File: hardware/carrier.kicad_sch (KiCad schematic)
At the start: 22 parts, among them J1 OPI_Z3_26PIN, J10 AUX 5V (screen), J14 BUCK 5V, J16 BATT 12V, J2 OPI_BREAKOUT, J3 UART5 ttyAS5, J4 UART2 ttyAS2, J8 I2C3 spare, J9 FAN 5V, Q1 IRF9540N

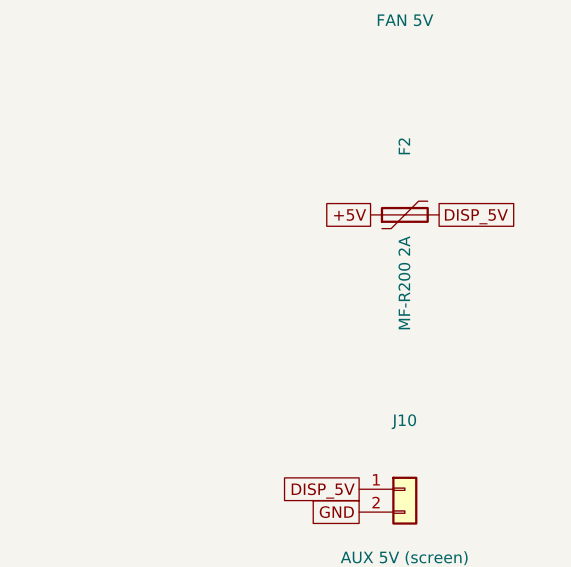
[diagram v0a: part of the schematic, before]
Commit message: chore: F2 MF-R200 -> MF-R250 (2.5A hold, same footprint)
Co-Authored-By: Claude Fable 5 <noreply@anthropic.com>
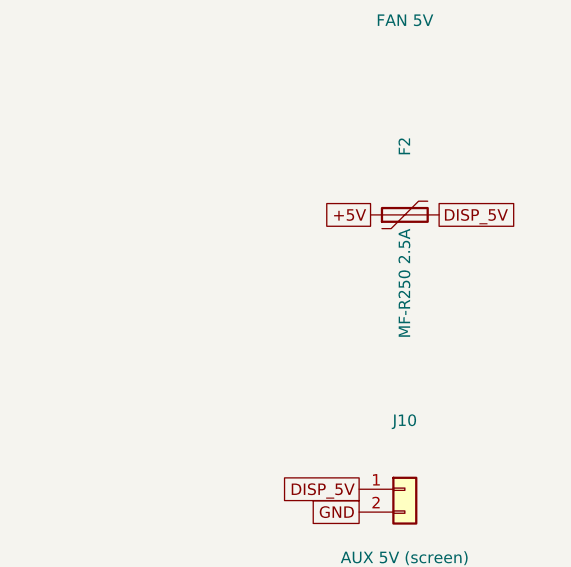
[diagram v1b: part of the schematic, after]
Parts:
- F2: value MF-R200 2A -> MF-R250 2.5A; MPN Bourns MF-R200 -> MF-R250
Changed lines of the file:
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@@
     (property "Reference" "F2" (at 369.57 207.01 0)
       (effects (font (size 1.27 1.27))))
-    (property "Value" "MF-R200 2A" (at 369.57 222.25 0)
+    (property "Value" "MF-R250 2.5A" (at 369.57 222.25 0)
       (effects (font (size 1.27 1.27))))
     (property "Footprint" "Fuse:Fuse_Bourns_MF-RG300" (at 369.57 214.63 0)
@@
     (property "Datasheet" "" (at 369.57 214.63 0)
       (effects (font (size 1.27 1.27)) (hide yes)))
-    (property "MPN" "Bourns MF-R200" (at 369.57 214.63 0)
+    (property "MPN" "MF-R250" (at 369.57 214.63 0)
       (effects (font (size 1.27 1.27)) (hide yes)))
     (pin "1")

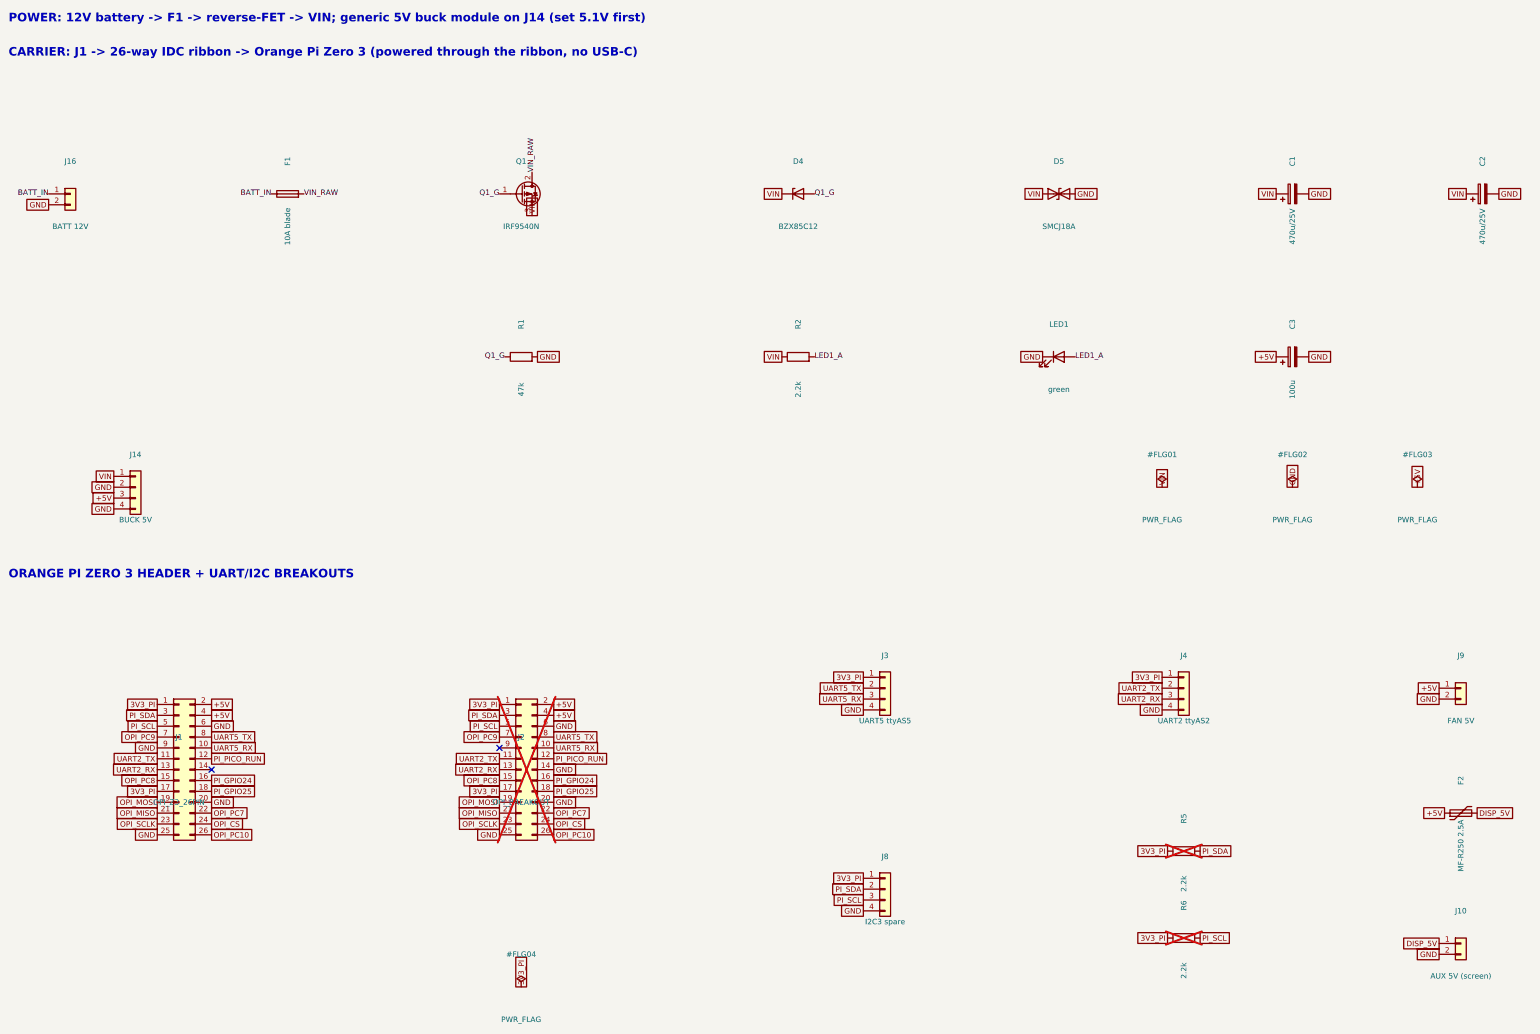
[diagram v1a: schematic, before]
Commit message: wip: v4.2 XL4015 daughterboard (pre-lays, ENC parts near J11, tab straps) + thrust-driver spec & net-spec draft
Co-Authored-By: Claude Fable 5 <noreply@anthropic.com>
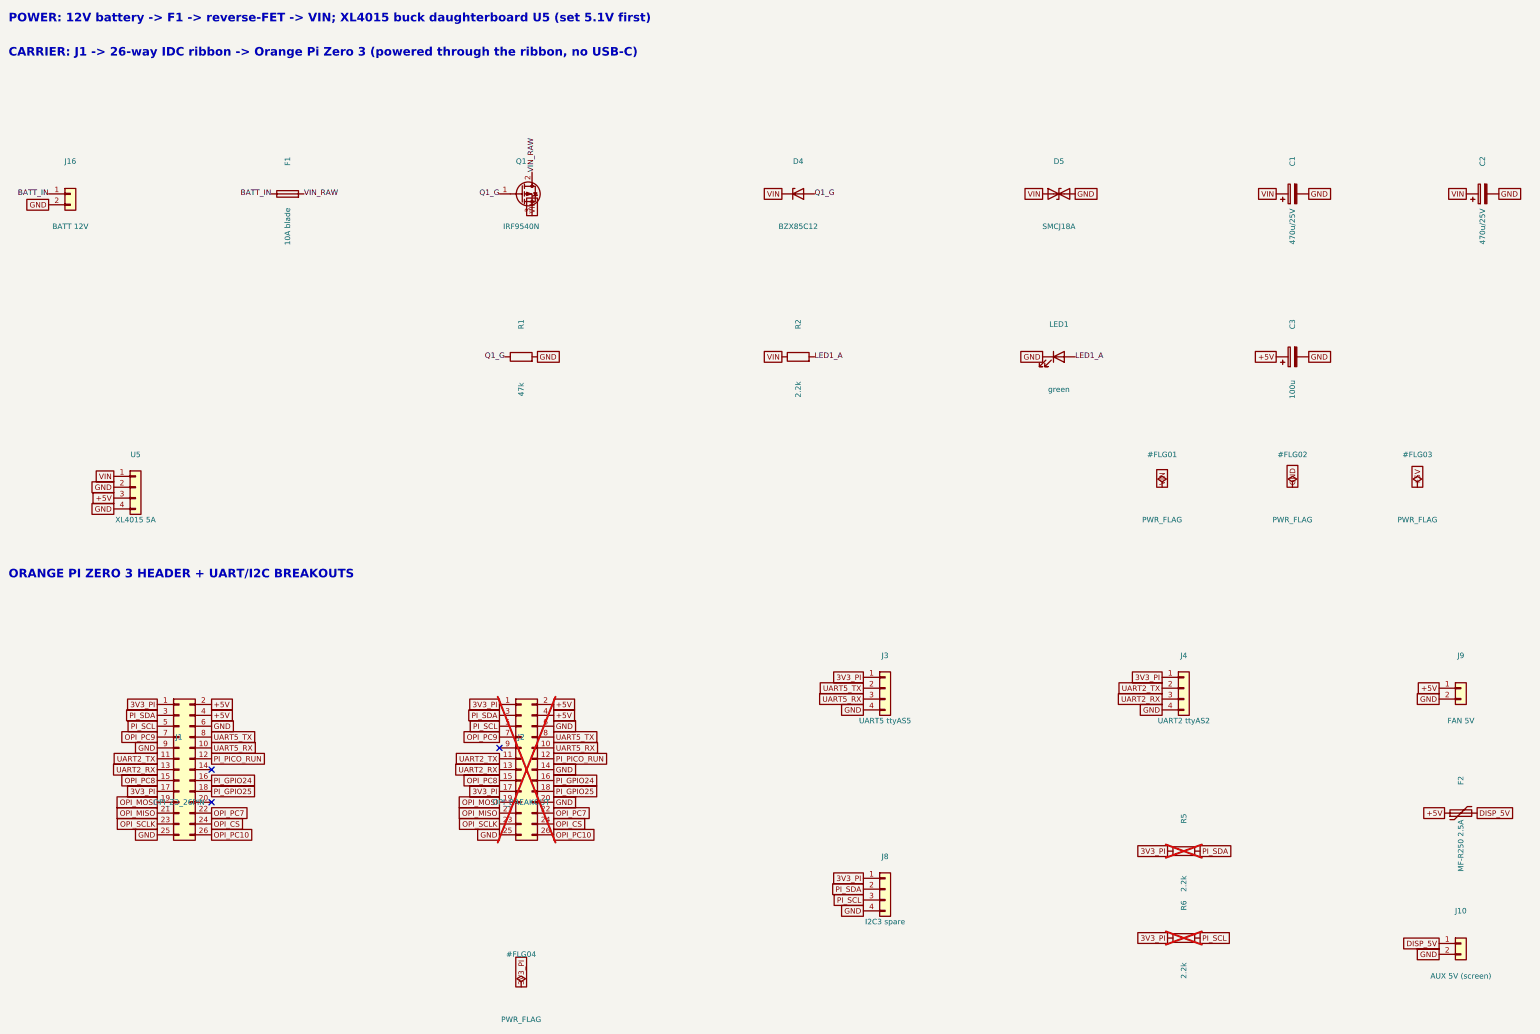
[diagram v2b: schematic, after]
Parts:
- removed J14: BUCK 5V, Connector_PinHeader_2.54mm:PinHeader_1x04_P2.54mm_Vertical, symbol Connector_Generic:Conn_01x04
- added U5: XL4015 5A, vanchor-helm:XL4015_Module, symbol Connector_Generic:Conn_01x04
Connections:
- net +5V: now also U5.3 (Pin_3)
- net GND: now also U5.2 (Pin_2), U5.4 (Pin_4); no longer J1.20 (Pin_20)
- net VIN: now also U5.1 (Pin_1)
- no-connect marks 2 -> 3
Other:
- note added: "POWER: 12V battery -> F1 -> reverse-FET -> VIN; XL4015 buck daughterboard U5 (set 5.1V first)"
- note removed: "POWER: 12V battery -> F1 -> reverse-FET -> VIN; generic 5V buck module on J14 (set 5.1V first)"
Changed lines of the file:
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@@
   (generator_version "8.0")
   (paper "A3")
-  (text "POWER: 12V battery -> F1 -> reverse-FET -> VIN; generic 5V buck module on J14 (set 5.1V first)" (exclude_from_sim no) (at 30 30 0)
+  (text "POWER: 12V battery -> F1 -> reverse-FET -> VIN; XL4015 buck daughterboard U5 (set 5.1V first)" (exclude_from_sim no) (at 30 30 0)
     (effects (font (size 2 2) (bold yes)) (justify left bottom))
   )
@@
   (symbol (lib_id "Connector_Generic:Conn_01x04") (at 59.69 138.43 0) (unit 1)
     (exclude_from_sim no) (in_bom yes) (on_board yes) (dnp no)
-    (property "Reference" "J14" (at 59.69 130.81 0)
-      (effects (font (size 1.27 1.27))))
-    (property "Value" "BUCK 5V" (at 59.69 146.05 0)
-      (effects (font (size 1.27 1.27))))
-    (property "Footprint" "Connector_PinHeader_2.54mm:PinHeader_1x04_P2.54mm_Vertical" (at 59.69 138.43 0)
+    (property "Reference" "U5" (at 59.69 130.81 0)
+      (effects (font (size 1.27 1.27))))
+    (property "Value" "XL4015 5A" (at 59.69 146.05 0)
+      (effects (font (size 1.27 1.27))))
+    (property "Footprint" "vanchor-helm:XL4015_Module" (at 59.69 138.43 0)
       (effects (font (size 1.27 1.27)) (hide yes)))
     (property "Datasheet" "" (at 59.69 138.43 0)
+      (effects (font (size 1.27 1.27)) (hide yes)))
+    (property "MPN" "XL4015 5A module (AliExpress)" (at 59.69 138.43 0)
       (effects (font (size 1.27 1.27)) (hide yes)))
     (pin "1")
@@
     (pin "3")
     (pin "4")
-    (instances (project "vanchor-helm" (path "/a0000000-0000-4000-8000-000000000001/c0000000-0000-4000-8000-000000000002" (reference "J14") (unit 1))))
+    (instances (project "vanchor-helm" (path "/a0000000-0000-4000-8000-000000000001/c0000000-0000-4000-8000-000000000002" (reference "U5") (unit 1))))
   )
   (symbol (lib_id "Device:C_Polarized") (at 330.2 107.95 90) (unit 1)
@@
       (effects (font (size 1.27 1.27)) (hide yes)))
   )
-  (global_label "GND" (shape passive) (at 77.47 212.09 0.0) (fields_autoplaced yes)
-    (effects (font (size 1.27 1.27)) (justify left))
-    (property "Intersheetrefs" "${INTERSHEET_REFS}" (at 77.47 212.09 0)
-      (effects (font (size 1.27 1.27)) (hide yes)))
-  )
   (global_label "OPI_MISO" (shape passive) (at 64.77 214.63 180.0) (fields_autoplaced yes)
     (effects (font (size 1.27 1.27)) (justify right))
@@
   )
   (no_connect (at 77.47 204.47))
+  (no_connect (at 77.47 212.09))
   (no_connect (at 144.78 199.39))
 )
